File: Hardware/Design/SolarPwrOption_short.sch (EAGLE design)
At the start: 19 parts, among them Q14 DMN3404L, Q14_ DMN3404L, Q15 DMN3404L, Q2 DMP4065S, Q3 BSS138, U2 OKI-78SR-5/1.5-W36-C

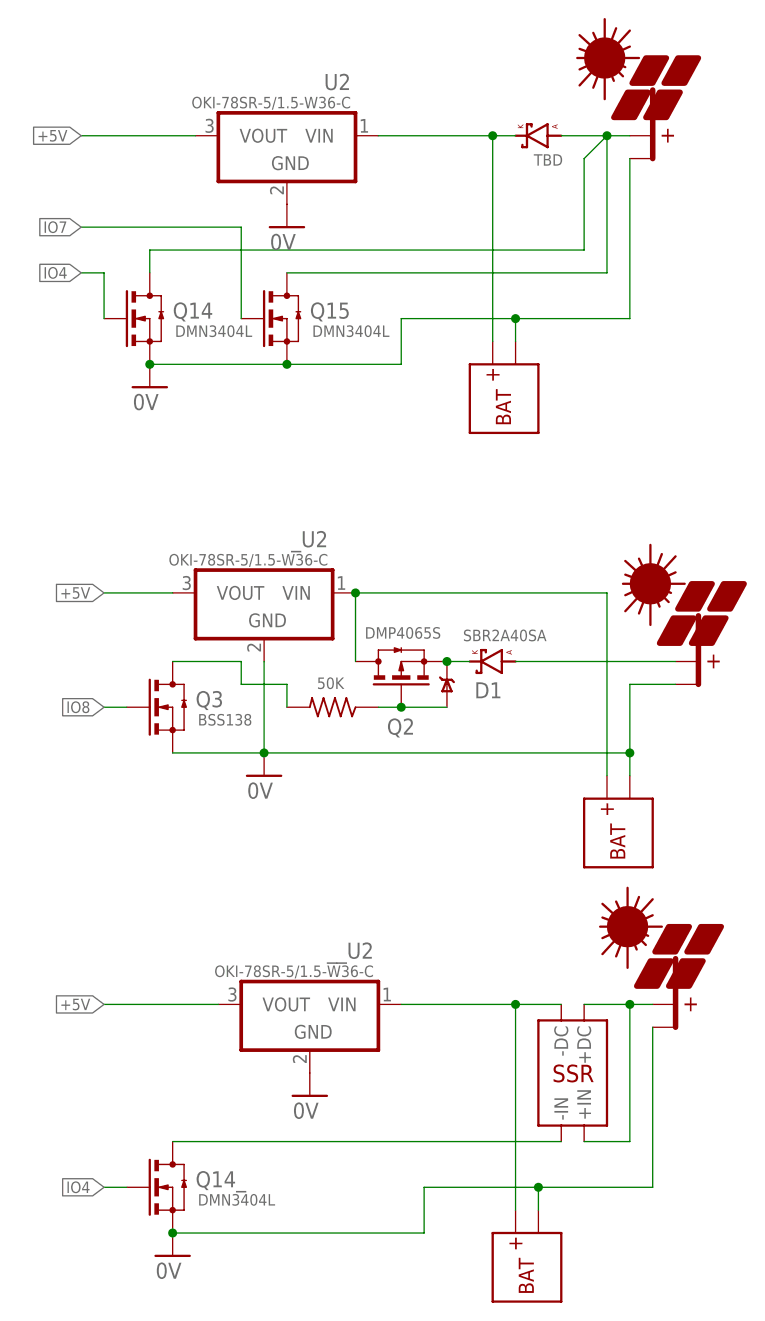
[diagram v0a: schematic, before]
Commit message: Hardware: set the solar pwr options in order
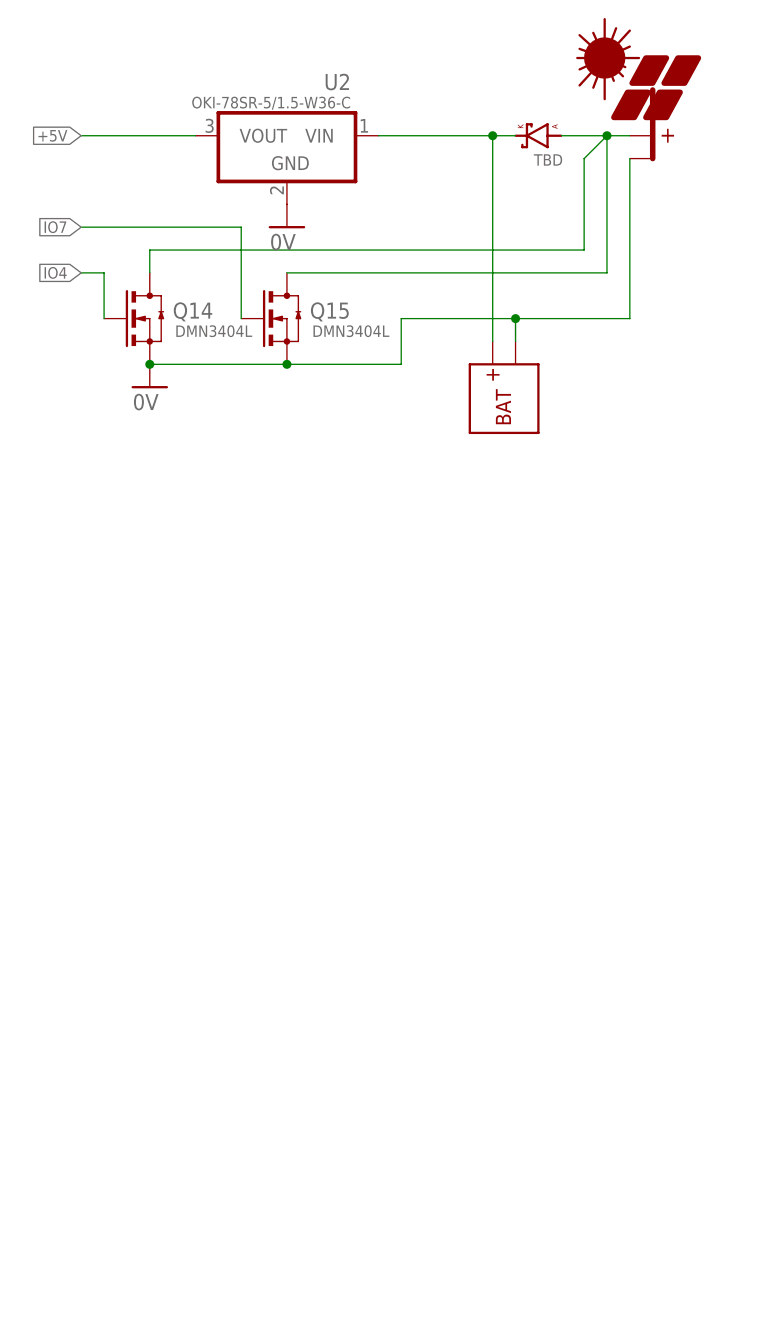
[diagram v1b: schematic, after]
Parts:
- removed D1: SBR2A40SA, D-SBR:DSMB
- removed D3: (no value), D-TVS:TVSSMC
- removed PV2, PV3: PV, Documentation:PV
- removed Q14_: DMN3404L, Q-NCH:N-CHDPAK
- removed Q2: DMP4065S, Q-PCH:N-CHDPAK
- removed Q3: BSS138, Q-NCH:N-CHDPAK
- removed R2: 50K, R-C:R0805
- removed U$1, U$2: BAT, Documentation:BAT
- removed U$3: SSR_DC, Documentation:SSR_DC
- removed _U2, __U2: OKI-78SR-5/1.5-W36-C, P-DCDC:OKI-78SR-H
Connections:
- removed net IO8: Q3.G
- removed net N$1: D1.K, D3.C, Q2.S
- removed net N$10: PV3.+PV, U$3.+DC, U$3.+IN
- removed net N$2: Q2.D, U$1.+BAT, _U2.VIN
- removed net N$3: D3.A, Q2.G, R2.1
- removed net N$5: Q3.D, R2.2
- removed net N$6: U$2.+BAT, U$3.-DC, __U2.VIN
- removed net N$7: D1.A, PV2.+PV
- removed net N$9: Q14_.D, U$3.-IN
- net +5V: no longer _U2.VOUT, __U2.VOUT
- net 0V: no longer PV2.-PV, PV3.-PV, Q14_.S, Q3.S, U$1.-BAT, U$2.-BAT, _U2.GND, __U2.GND
- net IO4: no longer Q14_.G
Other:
- note removed: "1.74A (Isc)"
- note removed: "17AHr"
- note removed: "2.92A (Isc)"
- note removed: "ALT"
- note removed: "AVR PIN"
- note removed: "DR06D06"
- note removed: "OPEN CIRCUIT OPTION"
- note removed: "OPEN CIRCUIT WITH SSR"
- note removed: "PWR"
- note removed: "SLP030-12U"
- note removed: "SLP045-12U"
- note removed: "WITHOUT BY-PASS DIODES"
